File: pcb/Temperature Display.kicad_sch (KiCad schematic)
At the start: 2 parts, among them P1 Connector_Generic:Conn_01x08, P2 Connector_Generic:Conn_01x08

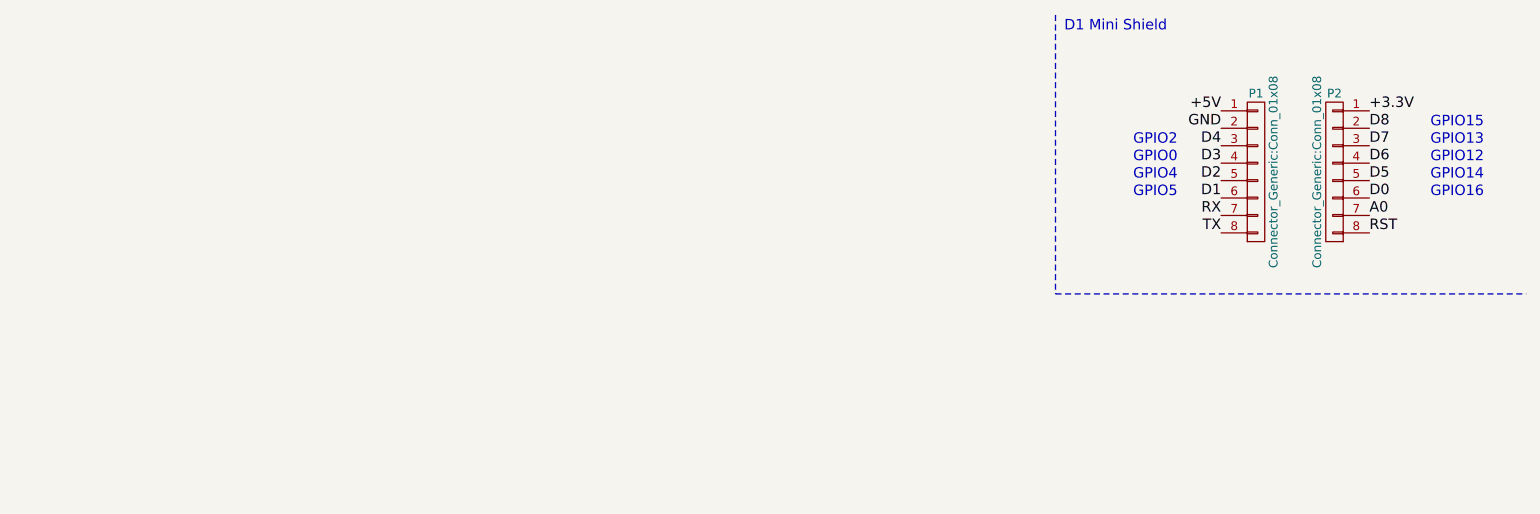
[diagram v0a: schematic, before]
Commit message: More PCB optimization, minor README fixes
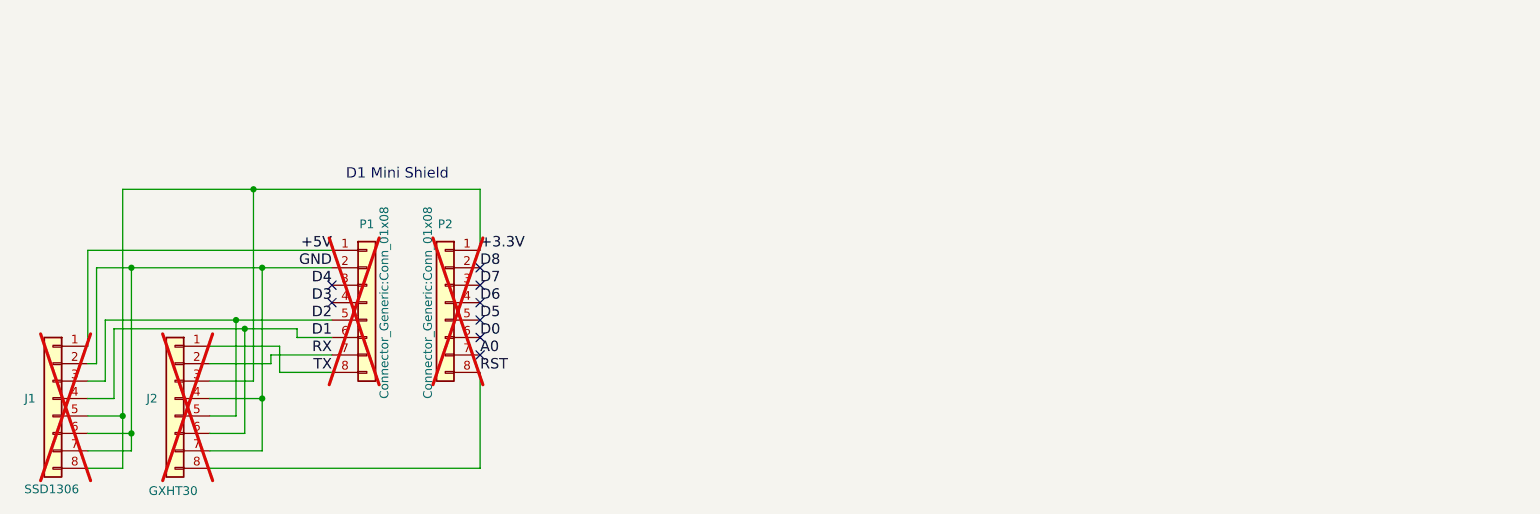
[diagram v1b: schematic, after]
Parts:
- added J1: SSD1306, Connector_PinHeader_2.54mm:PinHeader_1x08_P2.54mm_Vertical, symbol Connector_Generic:Conn_01x08
- added J2: GXHT30, Connector_PinHeader_2.54mm:PinHeader_1x08_P2.54mm_Vertical, symbol Connector_Generic:Conn_01x08
- P1, P2: footprint D1_mini:D1_mini_Pin_Header -> Connector_PinHeader_2.54mm:PinHeader_1x08_P2.54mm_Vertical; now not fitted
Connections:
- net +3.3V: now also J1.5 (Pin_5), J1.8 (Pin_8), J2.3 (Pin_3)
- net +5V: now also J1.1 (Pin_1)
- net D1: now also J1.4 (Pin_4), J2.6 (Pin_6)
- net D2: now also J1.3 (Pin_3), J2.5 (Pin_5)
- net GND: now also J1.2 (Pin_2), J1.6 (Pin_6), J1.7 (Pin_7), J2.4 (Pin_4), J2.7 (Pin_7)
- net RST: now also J2.8 (Pin_8)
- net RX: now also J2.2 (Pin_2)
- net TX: now also J2.1 (Pin_1)
- no-connect marks 0 -> 8
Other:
- note removed: "GPIO0"
- note removed: "GPIO12"
- note removed: "GPIO13"
- note removed: "GPIO14"
- note removed: "GPIO15"
- note removed: "GPIO16"
- note removed: "GPIO2"
- note removed: "GPIO4"
- note removed: "GPIO5"
- company: (none) -> Devcorner.nl
- title: (none) -> TemperatureDisplay
